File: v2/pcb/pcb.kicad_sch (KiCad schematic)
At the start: 14 parts, among them J1 LED STRIP, J2 RV3028, SW1 TIME, SW2 BRIGHTNESS, SW3 MODE, SW4 DAYLIGHT SAVING, U1 PRO MICRO

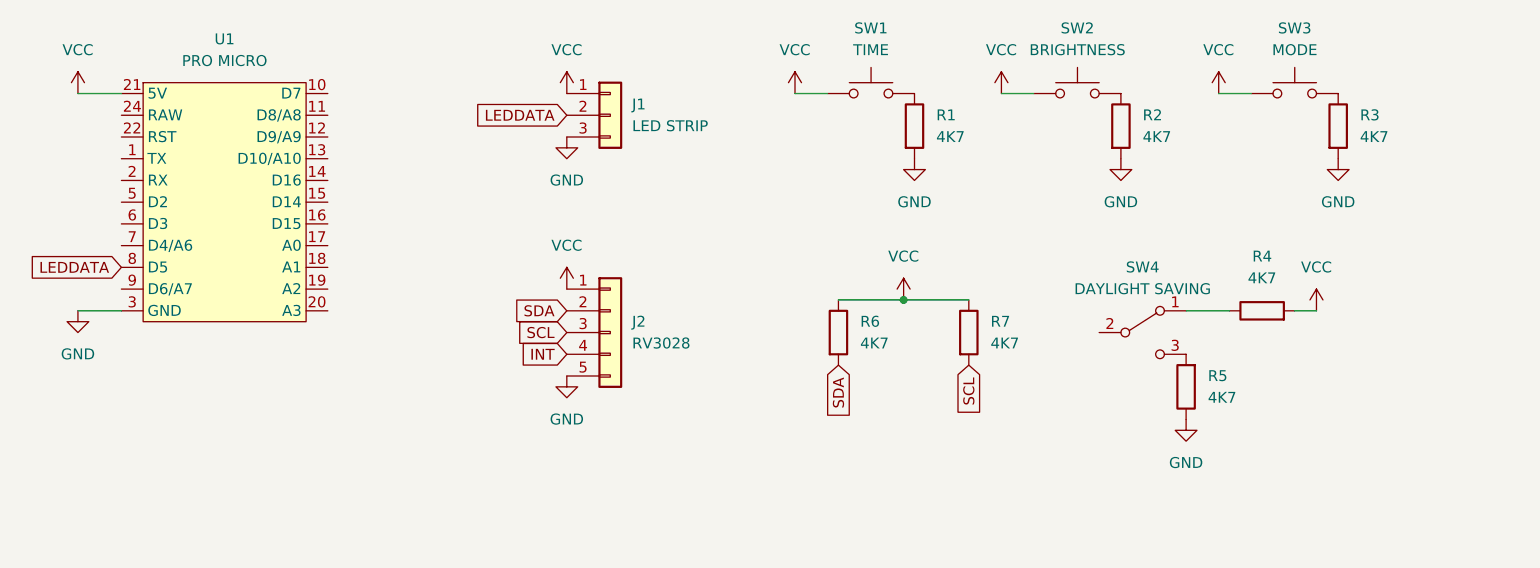
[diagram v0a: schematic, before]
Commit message: [PCB] New PCB mostly complete
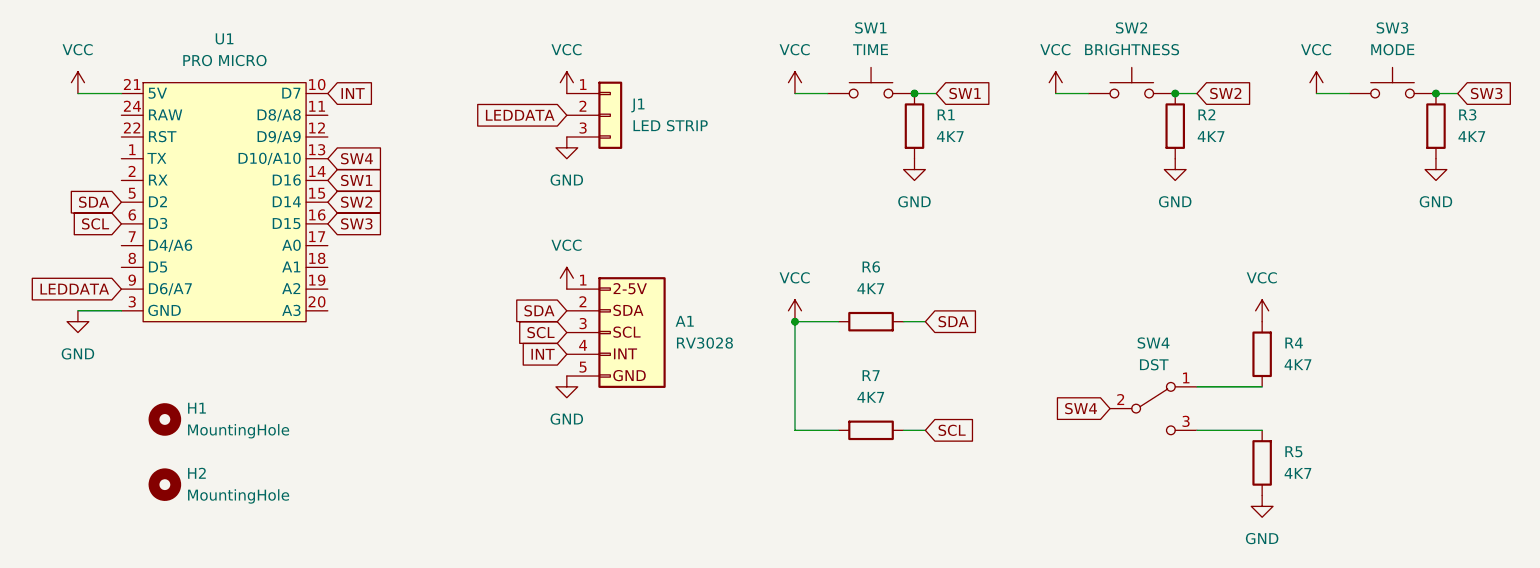
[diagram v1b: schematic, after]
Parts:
- removed J2: RV3028, Connector_PinHeader_2.54mm:PinHeader_1x05_P2.54mm_Vertical, symbol Connector_Generic:Conn_01x05
- added A1: RV3028, Pimoroni_RV3028:Pimoroni_RV3028_Breakout, symbol Pimoroni_RV3028:Pimoroni_RV3028_Breakout
- added H1, H2: MountingHole, MountingHole:MountingHole_3.2mm_M3_Pad, symbol Mechanical:MountingHole
- SW1, SW2, SW3: footprint SparkFun-Switch:Push_SMD_12x12mm -> SparkFun-Switch:Push_PTH_12x12mm
- SW4: value DAYLIGHT SAVING -> DST
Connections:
- net GND: now also A1.5 (Pin_5)
- net INT: now also U1.10 (D7), A1.4 (Pin_4)
- net LEDDATA: now also U1.9 (D6/A7); no longer U1.8 (D5)
- net SCL: now also R7.1, U1.6 (D3), A1.3 (Pin_3); no longer R7.2
- net SDA: now also U1.5 (D2), A1.2 (Pin_2)
- net VCC: now also R7.2, A1.1 (Pin_1); no longer R7.1
- net SW4: now reaches U1.13 (D10/A10)
- net SW4: now also SW4.2 (B)
- net SW1: now reaches U1.14 (D16)
- net SW1: now also R1.1, SW1.2
- net SW2: now reaches U1.15 (D14)
- net SW2: now also R2.1, SW2.2
- net SW3: now reaches U1.16 (D15)
- net SW3: now also R3.1, SW3.2
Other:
- moved on the sheet: R2, R3, R4, R5, R6, R7, SW2, SW3, SW4
